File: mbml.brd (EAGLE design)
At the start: 89.7 x 57.1 mm, 30 parts, among them K1 G5SB, Q1 2N2222, U1 LINEAR_REG_5V, U2 PHOTOCOUPLER, X1 43160-1102, X10 CON-2B2B-XH-A(LF)(SN), X2 CON-2, X3 CON-2B2B-XH-A(LF)(SN), X4 CON-2B2B-XH-A(LF)(SN), X5 CON-2B2B-XH-A(LF)(SN), X6 CON-2B2B-XH-A(LF)(SN), X7 CON-2B2B-XH-A(LF)(SN), X8 CON-2B2B-XH-A(LF)(SN), X9 CON-2B2B-XH-A(LF)(SN)

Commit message: Starting major overhaul
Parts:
- removed R9: 470, resistor:0204/5
- removed U2: PHOTOCOUPLER, TinkerTech:DIP-4
- added C1: (no value), SparkFun-Passives:CAP-PTH-SMALL
- added C2: (no value), TinkerTech:CAP-PTH-SMALL-POL
- R7: value 1.54k -> 1.5k
- X10: value CON-2B2B-XH-A(LF)(SN) -> CON_DB9VERT; device FVP:CON_2-2.5MM_TH -> TinkerTech:D09P24A4GV00LF
- moved U1 76.9 mm to (16.3, 62.4), turned to 0 degrees
- moved R8 75.6 mm to (25.1, 63.5), turned to 90 degrees
- moved X10 61.7 mm to (19.1, 6.60)
- moved X3 53.8 mm to (49.5, 5.08), turned to 0 degrees
- moved X4 52.8 mm to (40.6, 5.08), turned to 0 degrees
- moved R6 40.7 mm to (31.1, 43.2), turned to 270 degrees
- moved R5 32.9 mm to (55.6, 5.84), turned to 90 degrees
- moved K1 30.6 mm to (53.8, 21.2)
- moved D1 30.4 mm to (54.7, 32.1)
- moved X9 30.0 mm to (44.2, 16.4)
- moved Q1 29.9 mm to (63.2, 27.7), turned to 180 degrees
- moved R4 29.7 mm to (42.5, 10.2)
- moved R7 22.8 mm to (65.2, 35.1), turned to 270 degrees
- moved R3 19.8 mm to (39.4, 43.2), turned to 90 degrees
- moved X7 19.8 mm to (19.7, 24.8)
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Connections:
- net N$1 renamed D3
- net N$10 renamed D8
- net N$18 renamed D9
- net N$2 renamed D4
- net N$3 renamed TRANS_COLLECTOR
- net N$35 renamed D10
- net N$4 renamed D5
- net N$5 renamed TRANS_BASE
- net N$9 renamed D6
- removed net N$13: OK1.14, X6.P$1
- removed net N$46: R9.1, U2.1
- removed net N$47: R9.2, U$1.11
- removed net N$49: U2.3, X10.P$1
- new net A0: U$1.A0
- new net A1: U$1.A1
- new net A2: U$1.A2
- new net A3: U$1.A3
- new net A4: U$1.A4
- new net A5: U$1.A5
- new net A6: U$1.A6
- new net A7: U$1.A7
- new net AREF: U$1.AREF
- new net D11: U$1.11
- new net D12: U$1.12
- new net D13: U$1.13
- new net RST: U$1.RST
- new net RX: U$1.RX, X10.2
- new net TX: U$1.TX, X10.3
- net +12V: now also C1.1, OK1.14; no longer U2.4
- net +5V: now also C2.POS
- net GND: now also C1.2, C2.NEG, X10.5, X6.P$2; no longer U2.2, X10.P$2
- net N$14: now also X6.P$1; no longer X6.P$2
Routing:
- net RX: track 0.00 -> 127.8 mm, vias 0 -> 2
- net +5V: track 27.1 -> 111.6 mm, vias 1 -> 5
- net +12V: track 138.2 -> 65.9 mm
- net MON_PWR: track 18.7 -> 81.6 mm, vias 0 -> 1
- net D10: track 45.5 -> 0.00 mm, vias 0 -> 1
- net D3: track 41.1 -> 7.12 mm, vias 0 -> 1
- net MCU_VCC: track 27.1 -> 59.6 mm, vias 0 -> 1
- net A1: track 0.00 -> 28.7 mm, vias 0 -> 1
- net N$19: track 28.6 -> 0.00 mm
- net D11: track 0.00 -> 27.6 mm, vias 0 -> 1
- net A5: track 0.00 -> 27.6 mm, vias 0 -> 1
- net A3: track 0.00 -> 27.1 mm, vias 0 -> 1
- net A4: track 0.00 -> 27.1 mm, vias 0 -> 1
- net A2: track 0.00 -> 27.1 mm, vias 0 -> 1
- net AREF: track 0.00 -> 27.1 mm, vias 0 -> 1
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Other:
- board size 89.7 x 57.1 mm -> 69.8 x 91.4 mm
- board text removed: "PROJ SW"

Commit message: Ready for production
Hopefully…
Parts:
- removed X3, X4, X5, X6, X7, X8, X9: CON-2B2B-XH-A(LF)(SN), FVP:CON_2-2.5MM_TH
- added CPU_SW, FAN_PWR, MAIN_LED, MAIN_PWR, PROJ_LED, PROJ_PWR, SPKR_PWR, SPKR_SW, SPRK_SENSE: CON-2B2B-XH-A(LF)(SN), FVP:CON_2-2.5MM_TH
- added D2: (no value), TinkerTech:DO-201AD_AXIAL
- added L1: (no value), TinkerTech:RADIAL_8.5-DIA_5-SPACE
- added R10, R9: 470, resistor:0204/5
- C1: value (none) -> 100uF; device SparkFun-Passives:CAP-PTH-SMALL -> TinkerTech:RADIAL_POL_6.3-DIA_2.5-SPACE
- C2: value (none) -> 330uF; device TinkerTech:CAP-PTH-SMALL-POL -> TinkerTech:RADIAL_POL_10-DIA_5-SPACE
- R3: value 470 -> 10k
- R8: value 250k -> 470
- U1: value LINEAR_REG_5V -> REG_5V_SWITCHING_SI-8050E; device TinkerTech:DIP-8 -> TinkerTech:TO220F-5
- moved U1 60.8 mm to (53.0, 14.0)
- moved K1 53.1 mm to (20.7, 62.7), turned to 180 degrees
- moved C1 45.4 mm to (59.7, 27.9), turned to 0 degrees
- moved C2 41.4 mm to (40.6, 14.0), turned to 0 degrees
- moved Q1 40.5 mm to (36.6, 58.2)
- moved R5 38.2 mm to (44.7, 42.4), turned to 270 degrees
- moved R4 32.4 mm to (41.9, 42.5), turned to 90 degrees
- moved D1 32.4 mm to (30.6, 53.7)
- moved R7 29.6 mm to (36.6, 42.7)
- moved X10 27.9 mm to (38.1, 26.9)
- moved R8 25.3 mm to (39.4, 42.5)
- moved OK1 19.3 mm to (22.4, 14.0)
- moved R3 15.3 mm to (24.1, 41.9), turned to 270 degrees
- moved R2 5.12 mm to (47.4, 42.4)
- moved R1 5.12 mm to (50.2, 42.5)
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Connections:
- removed net D8: R3.2, U$1.8
- removed net N$12: OK1.12, X5.P$2
- removed net N$19: OK1.10, X8.P$1
- removed net N$20: OK1.9, X8.P$2
- removed net N$48: R8.1, U1.8
- new net AUX_1: OK1.10
- new net AUX_2: OK1.9
- new net N$1: D2.-, L1.P$1, U1.2
- new net N$2: OK1.5, R8.1
- new net N$3: R8.2, U$1.8
- new net N$4: OK1.11, SPKR_SW.P$1
- new net N$5: OK1.12, SPKR_SW.P$2
- net +12V: now also C1.+; no longer C1.1, U1.2, U1.3
- net +5V: now also C2.+, L1.P$2, SPKR_PWR.P$1, U1.4; no longer C2.POS, R8.2, U1.5, U1.6, U1.7, X9.P$1
- net D11: now also R3.2, SPRK_SENSE.P$1
- net D12: now also R10.2
- net D13: now also R9.2
- net D3: now also PROJ_PWR.P$2; no longer X4.P$2
- net D4: now also MAIN_PWR.P$2; no longer X3.P$2
- net GND: now also C1.-, C2.-, D2.+, FAN_PWR.P$2, MAIN_LED.P$2, MAIN_PWR.P$1, PROJ_LED.P$2, PROJ_PWR.P$1, SPKR_PWR.P$2, SPRK_SENSE.P$2, U1.3; no longer C1.2, C2.NEG, U1.4, X3.P$1, X4.P$1, X6.P$2, X9.P$2
- net MCU_VCC: now also R3.1
- net N$11: now also MAIN_LED.P$1, R10.1; no longer OK1.11, X5.P$1
- net N$14: now also FAN_PWR.P$1; no longer X6.P$1
- net N$15: now also CPU_SW.P$1; no longer X7.P$1
- net N$16: now also CPU_SW.P$2; no longer X7.P$2
- net N$6: now also PROJ_LED.P$1, R9.1; no longer OK1.5, R3.1
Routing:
- net GND: track 0.00 -> 177.6 mm, vias 4 -> 2
- net N$8: track 33.4 -> 145.1 mm
- net D3: track 7.12 -> 111.4 mm
- net N$1: track 0.00 -> 93.8 mm
- net RX: track 127.8 -> 39.3 mm, vias 2 -> 0
- net MON_PWR: track 81.6 -> 12.6 mm, vias 1 -> 0
- net +5V: track 111.6 -> 47.8 mm, vias 5 -> 1
- net N$7: track 0.00 -> 48.1 mm, vias 0 -> 1
- net N$5: track 0.00 -> 43.2 mm, vias 0 -> 1
- net N$2: track 0.00 -> 40.3 mm, vias 0 -> 1
- net N$4: track 0.00 -> 32.3 mm
- net D11: track 27.6 -> 58.4 mm
- net D12: track 26.7 -> 56.1 mm, vias 1 -> 0
- net A1: track 28.7 -> 0.00 mm, vias 1 -> 0
- net A5: track 27.6 -> 0.00 mm, vias 1 -> 0
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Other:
- board size 69.8 x 91.4 mm -> 69.8 x 69.8 mm
- board text added: "AUX_1"
- board text added: "AUX_2"
- board text removed: "+12V"
- board text removed: "10"
- board text removed: "11"
- board text removed: "12"
- board text removed: "13"
- board text removed: "3"
- board text removed: "4"
- board text removed: "5"
- board text removed: "6"
- board text removed: "8"
- board text removed: "9"
- board text removed: "A0"
- board text removed: "A1"
- board text removed: "A2"
- board text removed: "A3"
- board text removed: "A4"
- board text removed: "A5"
- board text removed: "AUX SW"
- board text removed: "Aref"
- board text removed: "BAT"
- board text removed: "BUS"
- board text removed: "CPU SW"
- board text removed: "FAN PR"
- board text removed: "MAIN BTN"
- board text removed: "PROJ BTN"
- board text removed: "RST"
- board text removed: "RX"
- board text removed: "SPKR SW"
- board text removed: "SPRK PR"
- board text removed: "TX"
- board text removed: "~"

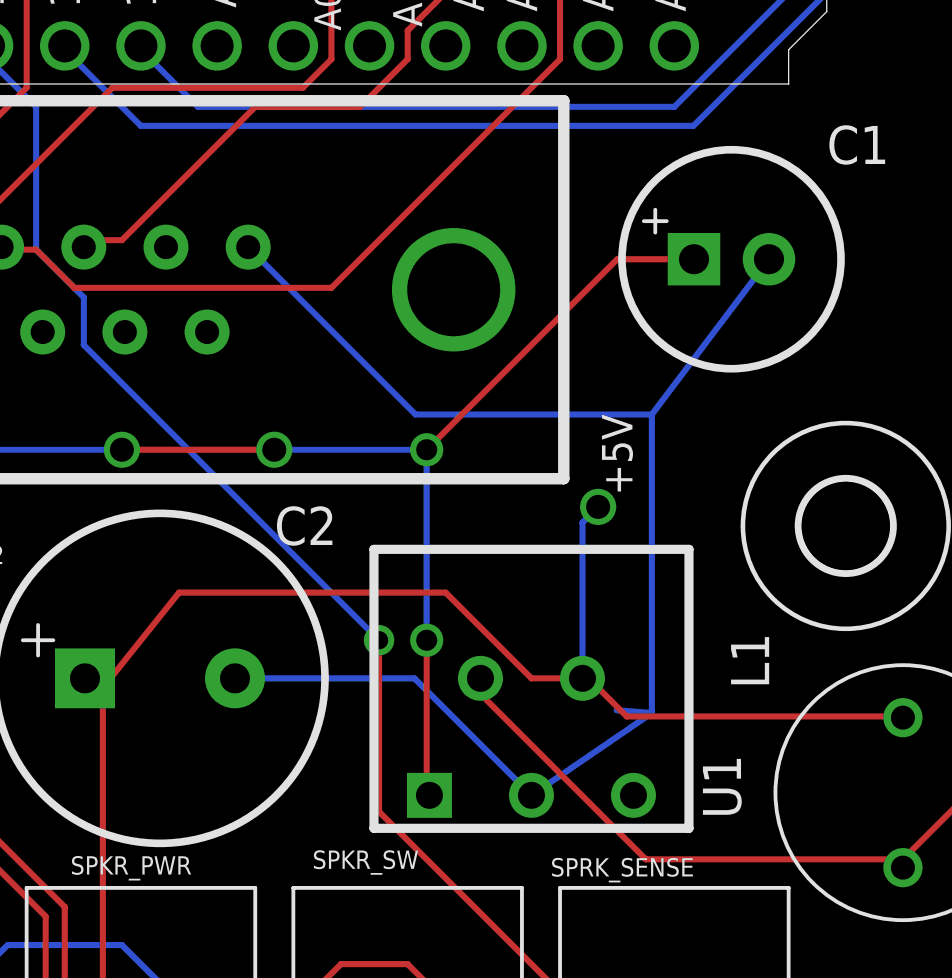
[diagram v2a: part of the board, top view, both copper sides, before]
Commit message: Fixed stray unconnected trace
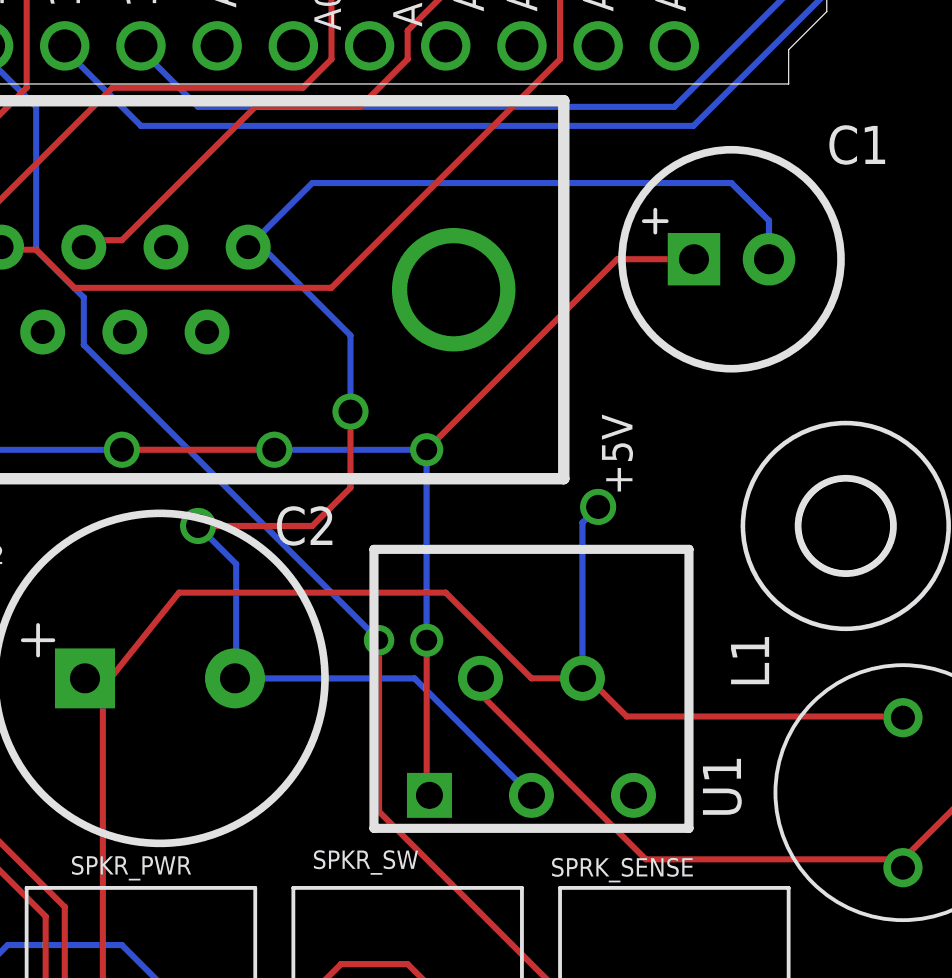
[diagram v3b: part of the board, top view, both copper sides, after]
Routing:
- net GND: track 177.6 -> 180.4 mm, vias 2 -> 4
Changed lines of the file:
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@@
 <wire x1="43.14" y1="13.97" x2="49.1225" y2="13.97" width="0.2032" layer="16"/>
 <wire x1="49.1225" y1="13.97" x2="53.0225" y2="10.07" width="0.2032" layer="16"/>
-<wire x1="55.86" y1="12.9075" x2="57.03625" y2="12.81375" width="0.2032" layer="16"/>
-<wire x1="57.03625" y1="12.81375" x2="53.0225" y2="10.07" width="0.2032" layer="16"/>
 <wire x1="49.41" y1="64.77" x2="43.18" y2="64.77" width="0.2032" layer="16"/>
 <wire x1="43.18" y1="64.77" x2="37.846" y2="59.436" width="0.2032" layer="16"/>
@@
 <wire x1="22.86" y1="55.88" x2="34.29" y2="55.88" width="0.2032" layer="16"/>
 <wire x1="34.29" y1="55.88" x2="34.925" y2="55.245" width="0.2032" layer="16"/>
-<wire x1="60.94" y1="27.94" x2="57.03625" y2="22.76625" width="0.2032" layer="16"/>
-<wire x1="57.03625" y1="22.76625" x2="57.03625" y2="12.81375" width="0.2032" layer="16"/>
-<wire x1="43.58" y1="28.344" x2="49.15775" y2="22.76625" width="0.2032" layer="16"/>
-<wire x1="49.15775" y1="22.76625" x2="57.03625" y2="22.76625" width="0.2032" layer="16"/>
 <wire x1="12.065" y1="3.175" x2="13.97" y2="1.27" width="0.2032" layer="1"/>
 <wire x1="13.97" y1="1.27" x2="16.51" y2="1.27" width="0.2032" layer="1"/>
@@
 <contactref element="PROJ_LED" pad="P$2"/>
 <contactref element="MAIN_LED" pad="P$2"/>
+<wire x1="43.58" y1="28.344" x2="45.716" y2="30.48" width="0.2032" layer="16"/>
+<wire x1="45.716" y1="30.48" x2="59.69" y2="30.48" width="0.2032" layer="16"/>
+<wire x1="59.69" y1="30.48" x2="60.94" y2="29.23" width="0.2032" layer="16"/>
+<wire x1="60.94" y1="29.23" x2="60.94" y2="27.94" width="0.2032" layer="16"/>
+<wire x1="43.14" y1="13.97" x2="43.18" y2="14.01" width="0.2032" layer="16"/>
+<wire x1="43.18" y1="14.01" x2="43.18" y2="17.78" width="0.2032" layer="16"/>
+<wire x1="43.18" y1="17.78" x2="41.91" y2="19.05" width="0.2032" layer="16"/>
+<via x="41.91" y="19.05" extent="1-16" drill="0.8"/>
+<wire x1="41.91" y1="19.05" x2="45.72" y2="19.05" width="0.2032" layer="1"/>
+<wire x1="45.72" y1="19.05" x2="46.99" y2="20.32" width="0.2032" layer="1"/>
+<wire x1="46.99" y1="20.32" x2="46.99" y2="22.86" width="0.2032" layer="1"/>
+<via x="46.99" y="22.86" extent="1-16" drill="0.8"/>
+<wire x1="46.99" y1="22.86" x2="46.99" y2="25.4" width="0.2032" layer="16"/>
+<wire x1="46.99" y1="25.4" x2="44.046" y2="28.344" width="0.2032" layer="16"/>
+<wire x1="44.046" y1="28.344" x2="43.58" y2="28.344" width="0.2032" layer="16"/>
 </signal>
 <signal name="D3">

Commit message: Version 2.1, DRC OK
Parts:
- removed H3: MOUNT-HOLE3.0, holes:3,0
- removed X10: CON_DB9VERT, TinkerTech:D09P24A4GV00LF
- added AUX_1, AUX_2, PROJ_BLANK: CON-2B2B-XH-A(LF)(SN), FVP:CON_2-2.5MM_TH
- added D3: 1N4004, diode:DO41-10
- added K2: 68800611622, Wurth_Wire_to_Board_Connectors_rev15d:68800611622
- added Q2: IRLZ24LPBF, transistor-power:TO262-V
- added R11: 100, resistor:0204/5
- added R12, R13: 10k, resistor:0204/5
- R9: value 470 -> 1.8k
- moved PROJ_PWR 81.7 mm to (64.8, 66.7), turned to 90 degrees
- moved H2 80.8 mm to (6.35, 6.35), turned to 180 degrees
- moved MAIN_PWR 72.2 mm to (56.5, 66.7), turned to 90 degrees
- moved K1 71.5 mm to (65.7, 7.11), turned to 0 degrees
- moved X2 65.8 mm to (66.0, 18.4), turned to 90 degrees
- moved H1 65.4 mm to (63.5, 50.8), turned to 180 degrees
- moved H4 65.4 mm to (6.35, 50.8), turned to 180 degrees
- moved SPKR_SW 64.6 mm to (36.8, 66.7), turned to 90 degrees
- moved CPU_SW 63.5 mm to (36.8, 57.8), turned to 90 degrees
- moved L1 54.0 mm to (17.1, 34.3)
- moved Q1 53.5 mm to (6.35, 14.0)
- moved FAN_PWR 52.3 mm to (56.5, 48.9), turned to 90 degrees
- moved SPRK_SENSE 50.3 mm to (36.8, 48.9), turned to 90 degrees
- moved D1 50.1 mm to (50.4, 7.75), turned to 90 degrees
- moved OK1 49.5 mm to (11.4, 62.2)
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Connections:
- removed net AUX_1: OK1.10
- removed net AUX_2: OK1.9
- new net N$10: Q2.2, R11.1, R12.1
- new net N$12: AUX_1.P$2, OK1.14
- new net N$13: AUX_1.P$1, OK1.13
- new net N$18: CPU_SW.P$1, OK1.9
- new net N$9: D3.A, FAN_PWR.P$2, Q2.1
- net +12V: now also D3.C, FAN_PWR.P$1; no longer OK1.14
- net A3: now also PROJ_BLANK.P$2, R13.1
- net A4: now also R11.2
- net GND: now also K2.5, PROJ_BLANK.P$1, Q2.3, R12.2; no longer FAN_PWR.P$2, X10.5
- net MCU_VCC: now also K2.6, R13.2
- net N$14: now also CPU_SW.P$2, OK1.10; no longer FAN_PWR.P$1, OK1.13
- net N$15: now also AUX_2.P$1; no longer CPU_SW.P$1
- net N$16: now also AUX_2.P$2; no longer CPU_SW.P$2
- net RX: now also K2.4; no longer X10.2
- net TX: now also K2.3; no longer X10.3
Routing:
- net N$8: track 145.1 -> 12.5 mm, vias 1 -> 0
- net MCU_VCC: track 32.4 -> 152.4 mm
- net TRANS_COLLECTOR: track 29.7 -> 116.5 mm
- net A3: track 0.00 -> 83.1 mm, vias 0 -> 2
- net N$1: track 93.8 -> 24.2 mm
- net N$9: track 0.00 -> 58.8 mm
- net +12V: track 84.6 -> 30.7 mm, vias 4 -> 2
- net D9: track 11.3 -> 62.7 mm
- net GND: track 180.4 -> 222.3 mm, vias 4 -> 3
- net N$7: track 48.1 -> 7.37 mm, vias 1 -> 0
- net D5: track 11.2 -> 45.3 mm
- net D3: track 111.4 -> 77.8 mm
- net N$12: track 0.00 -> 33.4 mm
- net N$17: track 38.4 -> 5.08 mm
- net N$2: track 40.3 -> 7.37 mm, vias 1 -> 0
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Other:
- board size 69.8 x 69.8 mm -> 74.9 x 72.4 mm
- board text added: "GND IN"
- board text added: "MBML1 CONTROL BOARD V2.1"
- board text removed: "+5V"
- board text removed: "AUX_1"
- board text removed: "AUX_2"
- board text removed: "GND"
- board text removed: "MBML1 CONTROL BOARD V2.0"
